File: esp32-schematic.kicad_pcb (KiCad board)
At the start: 2 copper layers, 26 parts, among them J1 GN-2630G, J2 Jumper, J3 Micro_SD_Card, U1 ESP32-S3-DEVKITC-1U-N8R2, U2 TJA1051T, U3 BME280, U4 MPU-9250

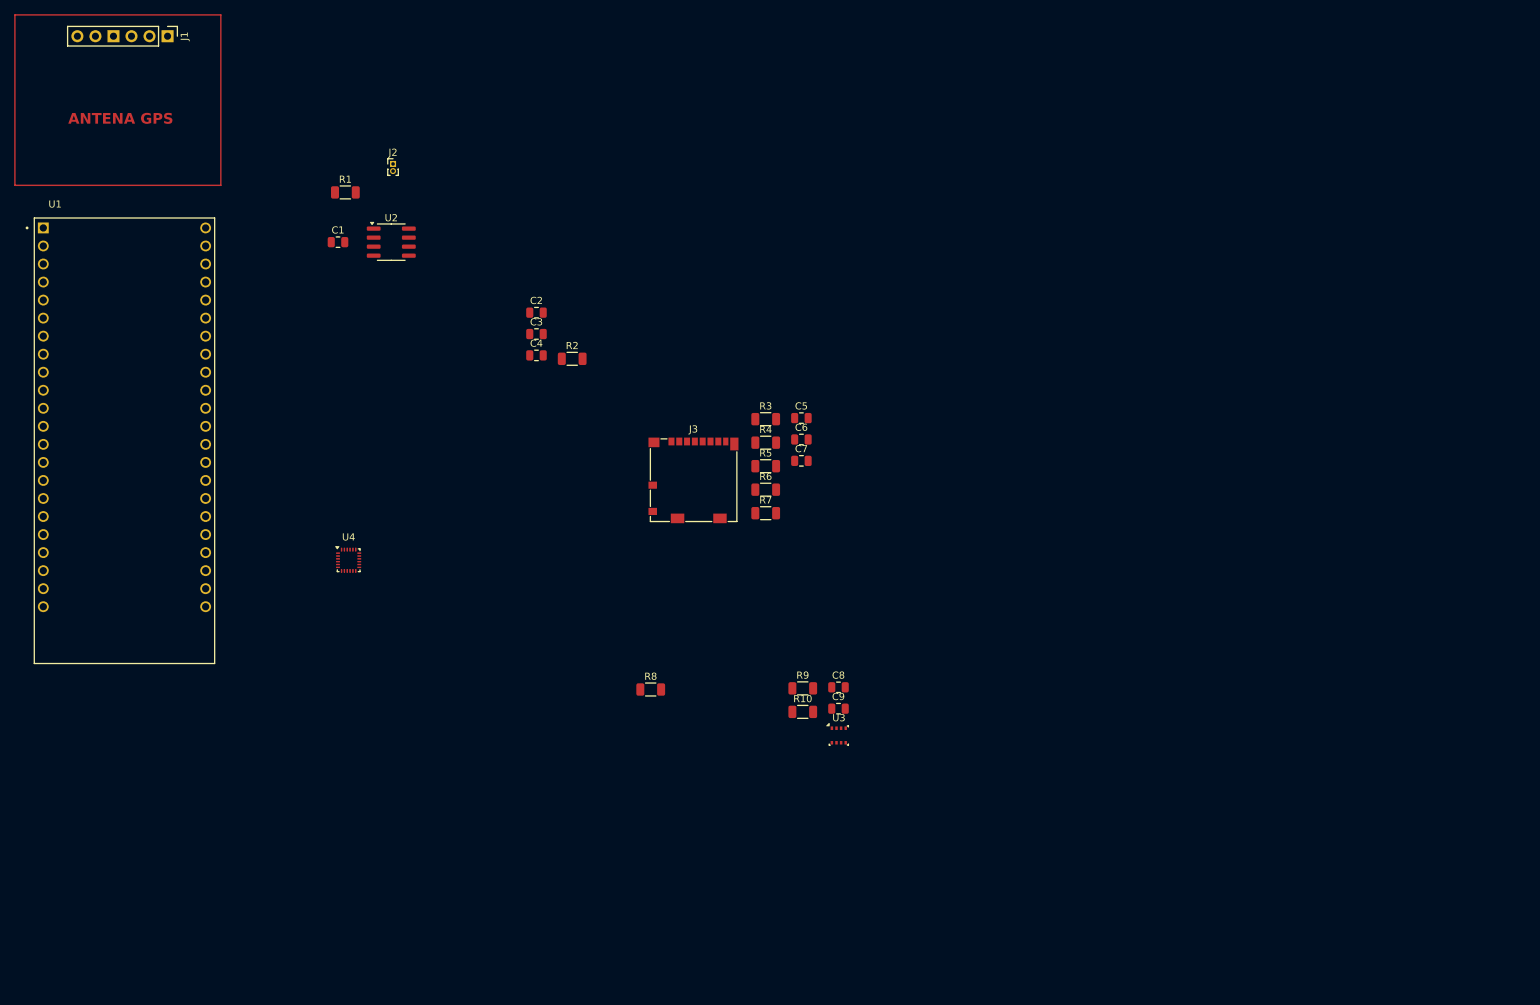
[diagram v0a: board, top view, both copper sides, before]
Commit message: DC-DC added, and bornes for the esp32 in progress
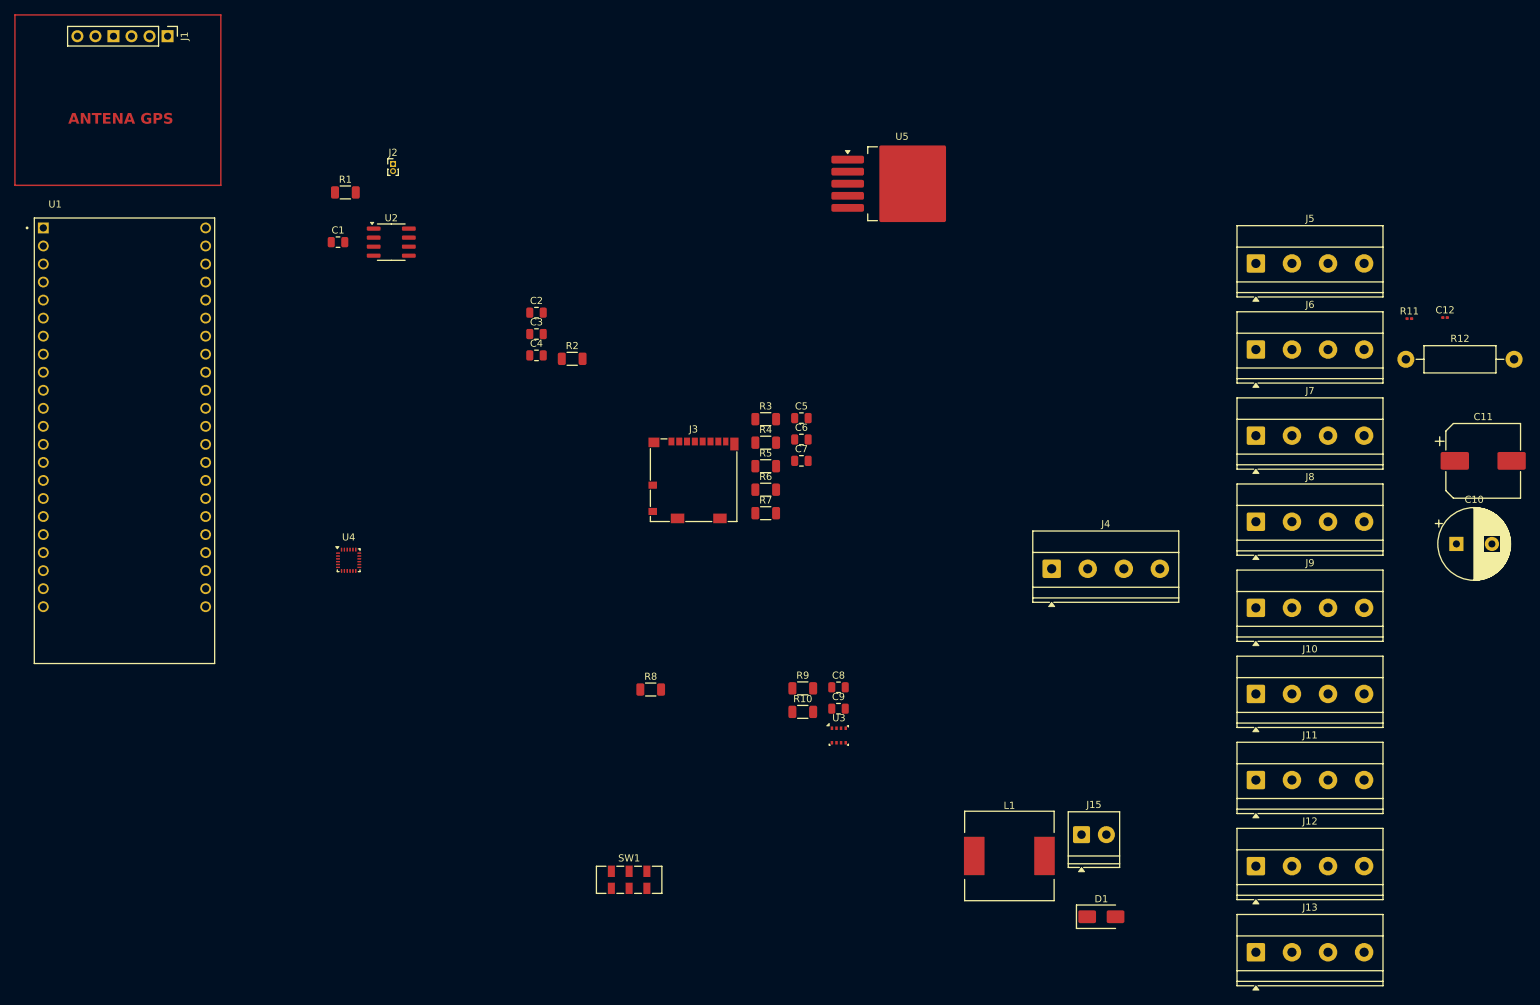
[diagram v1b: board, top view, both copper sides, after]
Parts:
- added C10: 470uF, Capacitor_THT:CP_Radial_D10.0mm_P5.00mm, F.Cu at (268.5, 89.0)
- added C11: 220uF, Capacitor_SMD:CP_Elec_10x10, F.Cu at (272.3, 77.3)
- added C12: 470pF, Capacitor_SMD:C_0201_0603Metric, F.Cu at (266.9, 57.1)
- added D1: 5V, Diode_SMD:D_SMA, F.Cu at (218.5, 141.5)
- added J10: Screw_Terminal_01x04, TerminalBlock_Phoenix:TerminalBlock_Phoenix_MKDS-1,5-4-5.08_1x04_P5.08mm_Horizontal, F.Cu at (240.3, 110.1)
- added J11: Screw_Terminal_01x04, TerminalBlock_Phoenix:TerminalBlock_Phoenix_MKDS-1,5-4-5.08_1x04_P5.08mm_Horizontal, F.Cu at (240.3, 122.2)
- added J12: Screw_Terminal_01x04, TerminalBlock_Phoenix:TerminalBlock_Phoenix_MKDS-1,5-4-5.08_1x04_P5.08mm_Horizontal, F.Cu at (240.3, 134.4)
- added J13: Screw_Terminal_01x04, TerminalBlock_Phoenix:TerminalBlock_Phoenix_MKDS-1,5-4-5.08_1x04_P5.08mm_Horizontal, F.Cu at (240.3, 146.5)
- added J15: POWER, TerminalBlock_Phoenix:TerminalBlock_Phoenix_PT-1,5-2-3.5-H_1x02_P3.50mm_Horizontal, F.Cu at (215.7, 129.9)
- added J4: Screw_Terminal_01x04, TerminalBlock_Phoenix:TerminalBlock_Phoenix_MKDS-1,5-4-5.08_1x04_P5.08mm_Horizontal, F.Cu at (211.5, 92.5)
- added J5: Screw_Terminal_01x04, TerminalBlock_Phoenix:TerminalBlock_Phoenix_MKDS-1,5-4-5.08_1x04_P5.08mm_Horizontal, F.Cu at (240.3, 49.5)
- added J6: Screw_Terminal_01x04, TerminalBlock_Phoenix:TerminalBlock_Phoenix_MKDS-1,5-4-5.08_1x04_P5.08mm_Horizontal, F.Cu at (240.3, 61.6)
- added J7: Screw_Terminal_01x04, TerminalBlock_Phoenix:TerminalBlock_Phoenix_MKDS-1,5-4-5.08_1x04_P5.08mm_Horizontal, F.Cu at (240.3, 73.8)
- added J8: Screw_Terminal_01x04, TerminalBlock_Phoenix:TerminalBlock_Phoenix_MKDS-1,5-4-5.08_1x04_P5.08mm_Horizontal, F.Cu at (240.3, 85.9)
- added J9: Screw_Terminal_01x04, TerminalBlock_Phoenix:TerminalBlock_Phoenix_MKDS-1,5-4-5.08_1x04_P5.08mm_Horizontal, F.Cu at (240.3, 98.0)
- added L1: 68uH, Inductor_SMD:L_12x12mm_H6mm, F.Cu at (205.5, 132.9)
- added R11: 1K, Resistor_SMD:R_0201_0603Metric, F.Cu at (261.9, 57.3)
- added R12: 3K, Resistor_THT:R_Axial_DIN0411_L9.9mm_D3.6mm_P15.24mm_Horizontal, F.Cu at (261.4, 63.0)
- added SW1: SW_SPDT, Button_Switch_SMD:SW_DPDT_CK_JS202011JCQN, F.Cu at (152.0, 136.3)
- added U5: LM2596S-5, Package_TO_SOT_SMD:TO-263-5_TabPin3, F.Cu at (190.4, 38.3)
